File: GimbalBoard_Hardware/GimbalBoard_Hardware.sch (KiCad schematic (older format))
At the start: 5 parts

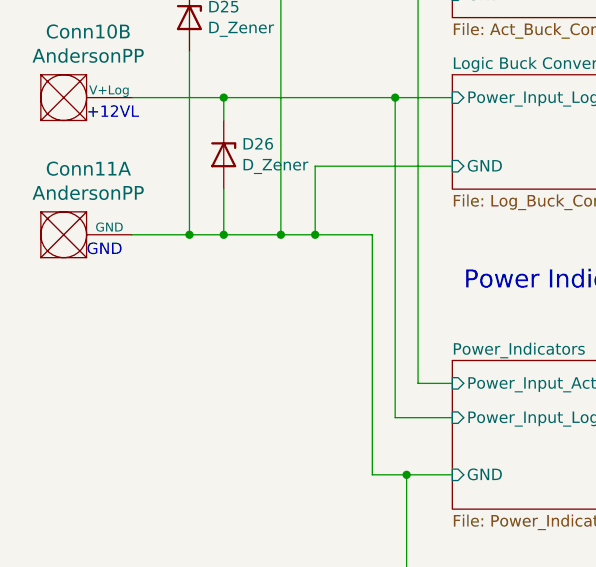
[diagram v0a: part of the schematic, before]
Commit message: sheet has been reviewed
schematic has been reviewed. and resister values have been changed. as well as a ground being added
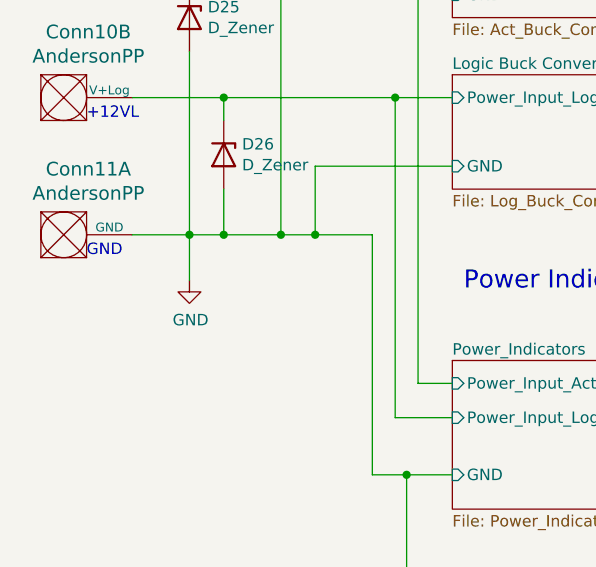
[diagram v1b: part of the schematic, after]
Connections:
- net Actuation Buck Converter/GND renamed GND
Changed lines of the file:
@@
 Wire Wire Line
 	2300 2500 2550 2500
+$Comp
+L power:GND #PWR?
+U 1 1 6163F6CB
+P 1400 3300
+F 0 "#PWR?" H 1400 3050 50  0001 C CNN
+F 1 "GND" H 1405 3127 50  0000 C CNN
+F 2 "" H 1400 3300 50  0001 C CNN
+F 3 "" H 1400 3300 50  0001 C CNN
+	1    1400 3300
+	1    0    0    -1
+$EndComp
+Wire Wire Line
+	1400 3300 1400 3100
 $EndSCHEMATC

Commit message: Post PDR changes
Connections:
- net Actuation Buck Converter/Power_Input_Act renamed Buck Converters/Power_Input_Act
- net Logic Buck Converter/Power_Input_Log renamed Buck Converters/Power_Input_Log
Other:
- note added: "Servo Connectors"
- note removed: "Power Indicators"
- note removed: "Servo Connectors\n"
- note removed: "Servo Indicators"
- moved on the sheet: Conn10B, Conn11A, Conn9C, D25, D26
